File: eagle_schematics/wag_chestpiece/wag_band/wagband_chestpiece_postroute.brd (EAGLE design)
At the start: 66 x 66 mm, 25 parts, among them U1 ATMEGA328P_PDIP, U2 TLV1117-33CDCY, U3 LM358DR, Y1 16MHz

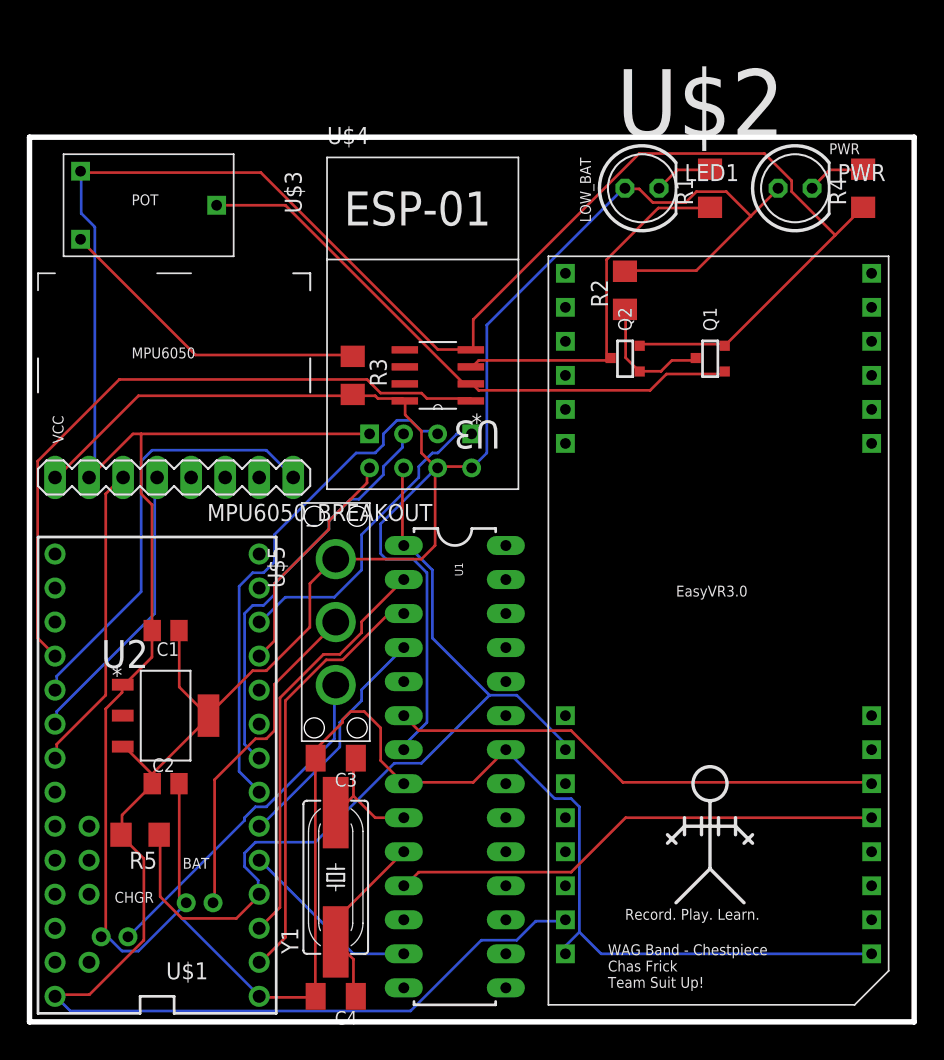
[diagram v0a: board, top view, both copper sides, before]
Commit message: Eagle schematic for chestpiece
Added new chestpiece with larger traces and everything good
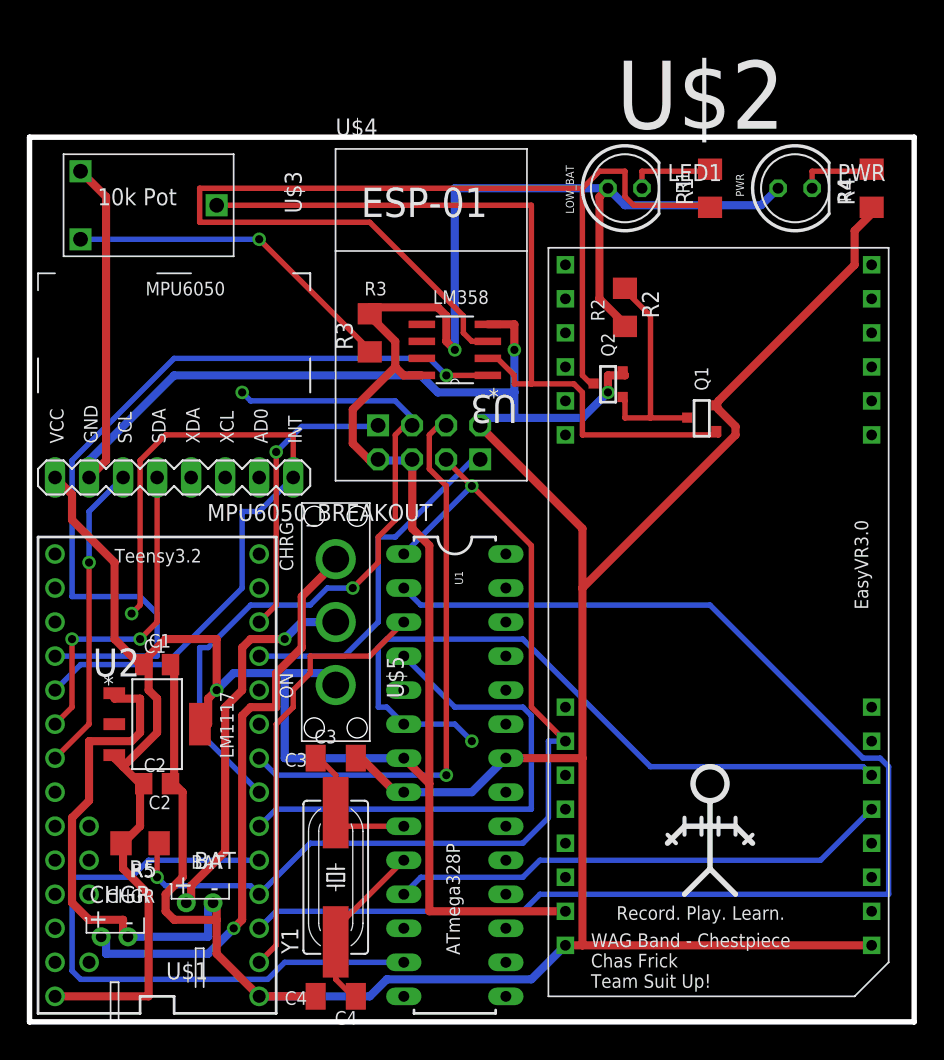
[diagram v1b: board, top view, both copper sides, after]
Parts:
- U$4: device esp8266modules:ESP01 -> mqp_custom_parts:ESP01
- moved Q1 4.49 mm to (50.2, 45.1)
- moved R3 3.42 mm to (25.4, 51.4), turned to 90 degrees
- moved C1 2.62 mm to (9.53, 26.7), turned to 0 degrees
- moved Q2 2.29 mm to (43.2, 47.6)
- moved U3 2.29 mm to (31.8, 50.2)
- moved LED1 1.27 mm to (44.5, 62.2)
- moved R2 1.27 mm to (44.5, 53.3), turned to 270 degrees
- moved U2 0.90 mm to (9.53, 22.2)
- moved U$4 0.90 mm to (29.8, 50.2)
- moved R4 0.64 mm to (62.9, 62.2)
- moved U1 0.64 mm to (31.8, 18.4)
- moved C2 0.63 mm to (9.53, 17.8)
- moved R5 0.63 mm to (8.26, 13.3)
- moved U$2 0.63 mm to (51.4, 31.1)
- flipped BAT to the top
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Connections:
- net !RST: now also U$4.RST; no longer U$4.CH_PD
- net GND: now also U$4.RX; no longer U$4.GND
- net N$18: now also U$4.GPIO0; no longer U$4.GPIO2
- net N$19: now also U$4.VCC; no longer U$4.TX
- net N$2: now also U$4.GND; no longer U$4.RX
- net N$7: now also U$4.GPIO2; no longer U$4.GPIO0
- net VCC: now also U$4.CH_PD, U$4.TX; no longer U$4.RST, U$4.VCC
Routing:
- net N$13: track 31.2 -> 99.3 mm
- net N$10: track 28.0 -> 84.5 mm
- net N$16: track 13.7 -> 47.0 mm
- net N$8: track 32.4 -> 54.8 mm, vias 0 -> 1
- net N$1: track 17.9 -> 39.2 mm
- net N$25: track 25.7 -> 43.8 mm, vias 0 -> 1
- net N$6: track 37.0 -> 53.8 mm, vias 0 -> 1
- net N$7: track 38.0 -> 54.2 mm, vias 0 -> 2
- net N$4: track 44.3 -> 59.0 mm
- net GND: track 289.0 -> 302.8 mm, vias 0 -> 2
- net N$14: track 50.7 -> 62.6 mm, vias 0 -> 1
- net N$18: track 30.5 -> 41.9 mm, vias 0 -> 1
- net VCC: track 225.4 -> 216.4 mm, vias 0 -> 2
- net N$19: track 17.5 -> 26.3 mm
- net N$9: track 9.69 -> 16.7 mm
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- added copper zone on layer 1, net N$24
- added copper zone on layer 16, net N$26
- removed copper zone on layer 1, net GND
- removed copper zone on layer 16, net GND
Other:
- board text added: "AD0"
- board text added: "ATmega328P"
- board text added: "C1"
- board text added: "C2"
- board text added: "C3"
- board text added: "C4"
- board text added: "CHRG"
- board text added: "GND"
- board text added: "INT"
- board text added: "LM1117"
- board text added: "LM358"
- board text added: "ON"
- board text added: "R1"
- board text added: "R2"
- board text added: "R3"
- board text added: "R4"
- board text added: "R5"
- board text added: "SCL"
- board text added: "SDA"
- board text added: "Teensy3.2"
- board text added: "XCL"
- board text added: "XDA"
- board text removed: "POT"

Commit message: Fixed all schematics and boards to have separate power supplies finally :100:
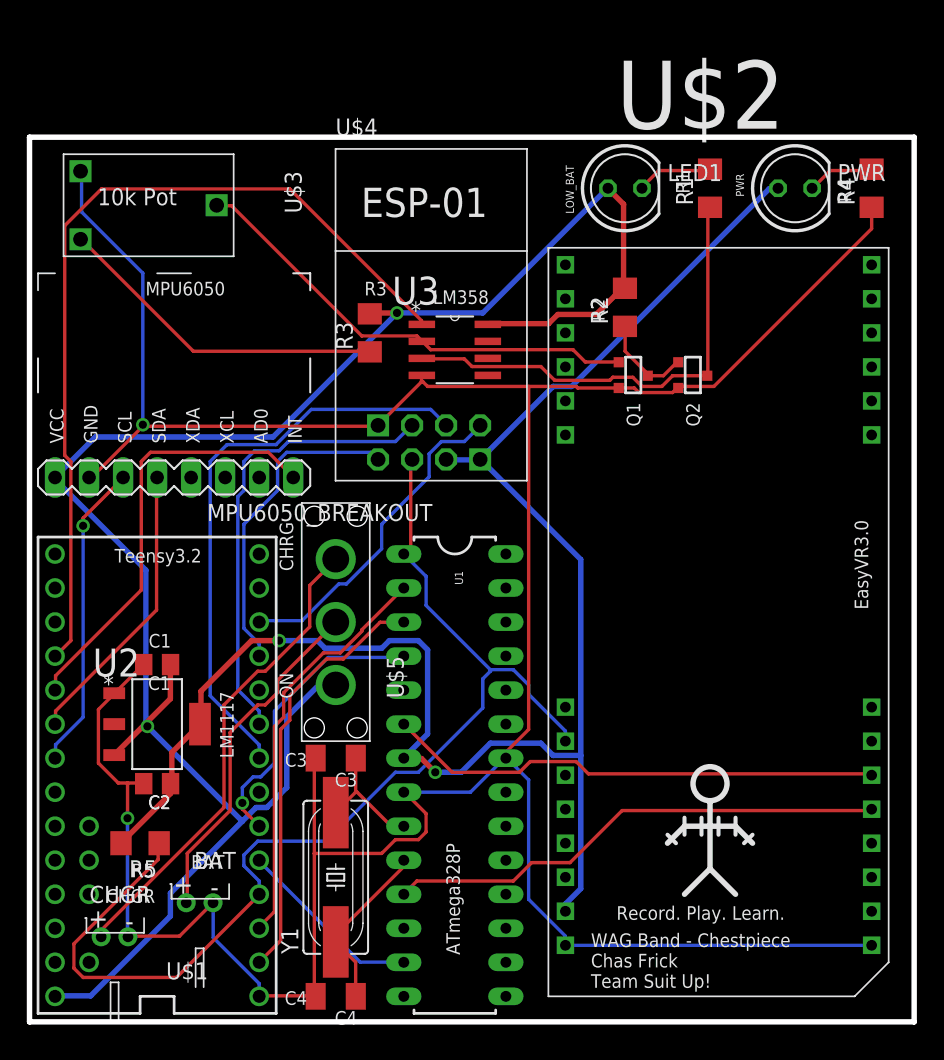
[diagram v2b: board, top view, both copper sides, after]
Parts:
- moved Q2 6.38 mm to (49.5, 48.3), turned to 270 degrees
- moved Q1 5.99 mm to (45.1, 48.3), turned to 270 degrees
- turned C1 to 180 degrees
- turned C2 to 180 degrees
- turned C3 to 180 degrees
- turned R2 to 90 degrees
- turned U3 to 0 degrees
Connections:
- removed net N$7: U$1.5, U$4.GPIO2
- removed net VCC: C1.1, C2.1, LED1.A, MPU6050_BREAKOUT.VCC, PWR.A, R2.2, R3.2, R5.2, U$1.VIN, U$2.P$13, U$4.CH_PD, U$4.TX, U$5.P$1, U1.7, U2.3, U2.4, U3.8
- new net +3V3: C2.1, PWR.A, R5.2, U$2.P$13, U$4.RST, U$4.VCC, U1.7, U2.4
- new net N$24: U$1.7, U$4.GPIO2
- new net V+: C1.1, LED1.A, MPU6050_BREAKOUT.VCC, R2.2, R3.2, U$1.VIN, U$5.P$1, U2.3, U3.8
- net !RST: now also U$4.CH_PD; no longer U$4.RST
- net GND: now also U$4.GND; no longer U$4.RX
- net N$19: now also U$4.TX; no longer U$4.VCC
- net N$2: now also U$4.RX; no longer U$4.GND
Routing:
- net VCC: track 216.4 -> 0.00 mm, vias 2 -> 0
- net V+: track 0.00 -> 146.5 mm, vias 0 -> 2
- net +3V3: track 0.00 -> 127.3 mm, vias 0 -> 2
- net N$13: track 99.3 -> 30.6 mm
- net GND: track 302.8 -> 240.7 mm
- net N$7: track 54.2 -> 0.00 mm, vias 2 -> 0
- net N$10: track 84.5 -> 35.4 mm
- net N$24: track 0.00 -> 34.1 mm
- net N$16: track 47.0 -> 14.0 mm
- net N$4: track 59.0 -> 34.9 mm
- net N$8: track 54.8 -> 32.1 mm, vias 1 -> 0
- net N$1: track 39.2 -> 21.8 mm, vias 0 -> 1
- net N$6: track 53.8 -> 37.2 mm, vias 1 -> 0
- net !RST: track 73.7 -> 84.9 mm, vias 2 -> 0
- net N$9: track 16.7 -> 7.11 mm
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- removed copper zone on layer 1, net N$24
- removed copper zone on layer 16, net N$26
